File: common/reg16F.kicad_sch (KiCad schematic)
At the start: 8 parts, among them U17 74AHC1G08, U18 SN74AHC16374DGGR

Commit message: Updated ALU and moved common schematics to common/ for enhanced reusability
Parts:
- U17: footprint Package_TO_SOT_SMD:SOT-353_SC-70-5 -> Package_TO_SOT_SMD:SOT-23-5
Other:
- title: (none) -> 16-bit Register
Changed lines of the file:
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@@
 	(paper "A4")
 	(title_block
+		(title "16-bit Register")
 		(rev "V1.0")
+		(comment 1 "Designed to be used as a drop-in replacement to 4 74LS173 ICs used together")
 	)
 	(junction
@@
 		)
 		(instances
-			(project ""
+			(project "ALU"
 				(path "/c0bb03ae-ed0c-4e9e-9f7c-15f29fb8b868/e88f18b5-e72c-4b0e-9142-9a24ab457305"
 					(reference "TP2")
@@
 			)
 		)
-		(property "Footprint" "Package_TO_SOT_SMD:SOT-353_SC-70-5"
+		(property "Footprint" "Package_TO_SOT_SMD:SOT-23-5"
 			(at 81.915 126.365 0)
 			(effects

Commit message: Made tri-state and register schematic look nice
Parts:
- removed U18: SN74AHC16374DGGR, Package_SO:TSSOP-48_6.1x12.5mm_P0.5mm, symbol 74FCT16374CTPVG:74FCT16374CTPVG
- added U2: SN74AHCT16374DGGR, Package_SO:TSSOP-48_6.1x12.5mm_P0.5mm, symbol 74FCT16374CTPVG:74FCT16374CTPVG
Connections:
- net +5V: now also U2.18 (VCC_2), U2.31 (VCC), U2.42 (VCC_4), U2.7 (VCC_1)
- net DIN0: now also U2.23 (2Q8)
- net DIN1: now also U2.22 (2Q7)
- net DIN10: now also U2.9 (1Q6)
- net DIN11: now also U2.8 (1Q5)
- net DIN12: now also U2.6 (1Q4)
- net DIN13: now also U2.5 (1Q3)
- net DIN14: now also U2.3 (1Q2)
- net DIN15: now also U2.2 (1Q1)
- net DIN2: now also U2.20 (2Q6)
- net DIN3: now also U2.19 (2Q5)
- net DIN4: now also U2.17 (2Q4)
- net DIN5: now also U2.16 (2Q3)
- net DIN6: now also U2.14 (2Q2)
- net DIN7: now also U2.13 (2Q1)
- net DIN8: now also U2.12 (1Q8)
- net DIN9: now also U2.11 (1Q7)
- net DOUT0: now also U2.26 (2D8)
- net DOUT1: now also U2.27 (2D7)
- net DOUT10: now also U2.40 (1D6)
- net DOUT11: now also U2.41 (1D5)
- net DOUT12: now also U2.43 (1D4)
- net DOUT13: now also U2.44 (1D3)
- net DOUT14: now also U2.46 (1D2)
- net DOUT15: now also U2.47 (1D1)
- net DOUT2: now also U2.29 (2D6)
- net DOUT3: now also U2.30 (2D5)
- net DOUT4: now also U2.32 (2D4)
- net DOUT5: now also U2.33 (2D3)
- net DOUT6: now also U2.35 (2D2)
- net DOUT7: now also U2.36 (2D1)
- net DOUT8: now also U2.37 (1D8)
- net DOUT9: now also U2.38 (1D7)
- net GND: now also U2.10 (GND_2), U2.15 (GND_3), U2.21 (GND_4), U2.28 (GND), U2.34 (GND_6), U2.39 (GND_7), U2.4 (GND_1), U2.45 (GND_8)
- net ~{OE}: now also U2.25 (2CLK), U2.48 (1CLK)
- net at TP2.1, U17.4: now also U2.1 (1~{OE}), U2.24 (2~{OE})
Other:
- moved on the sheet: C24, C25, C26, C27, C28, TP2, U17

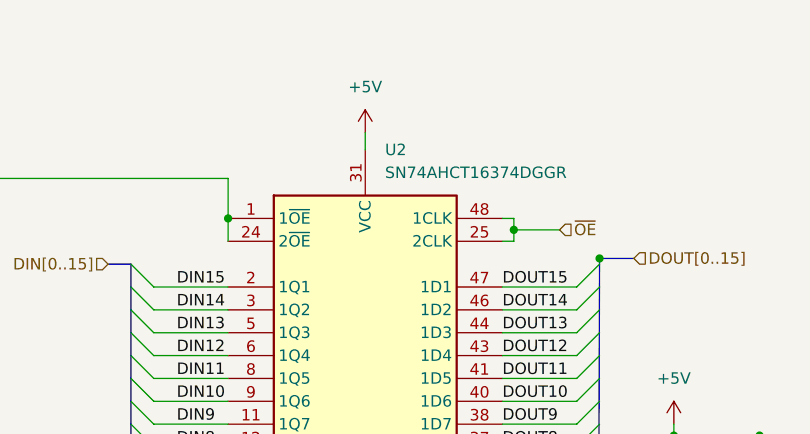
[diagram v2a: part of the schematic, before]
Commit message: Fixed silkscreen on ALU and Double Buffer
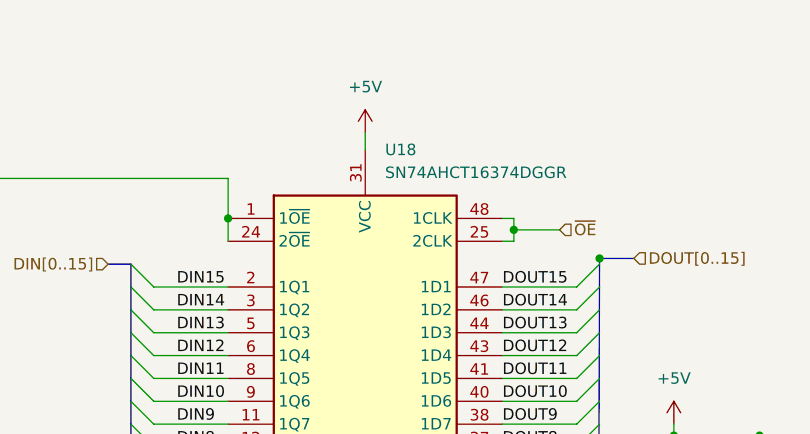
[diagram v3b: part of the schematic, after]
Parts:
- renumbered U2 to U18
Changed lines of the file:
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@@
 		(dnp no)
 		(fields_autoplaced yes)
-		(property "Reference" "#PWR040"
+		(property "Reference" "#PWR041"
 			(at 107.315 116.84 0)
 			(effects
@@
 		(dnp no)
 		(fields_autoplaced yes)
-		(property "Reference" "U2"
+		(property "Reference" "U18"
 			(at 109.5091 48.26 0)
 			(effects
@@
 		(dnp no)
 		(fields_autoplaced yes)
-		(property "Reference" "#PWR036"
+		(property "Reference" "#PWR037"
 			(at 107.315 50.165 0)
 			(effects

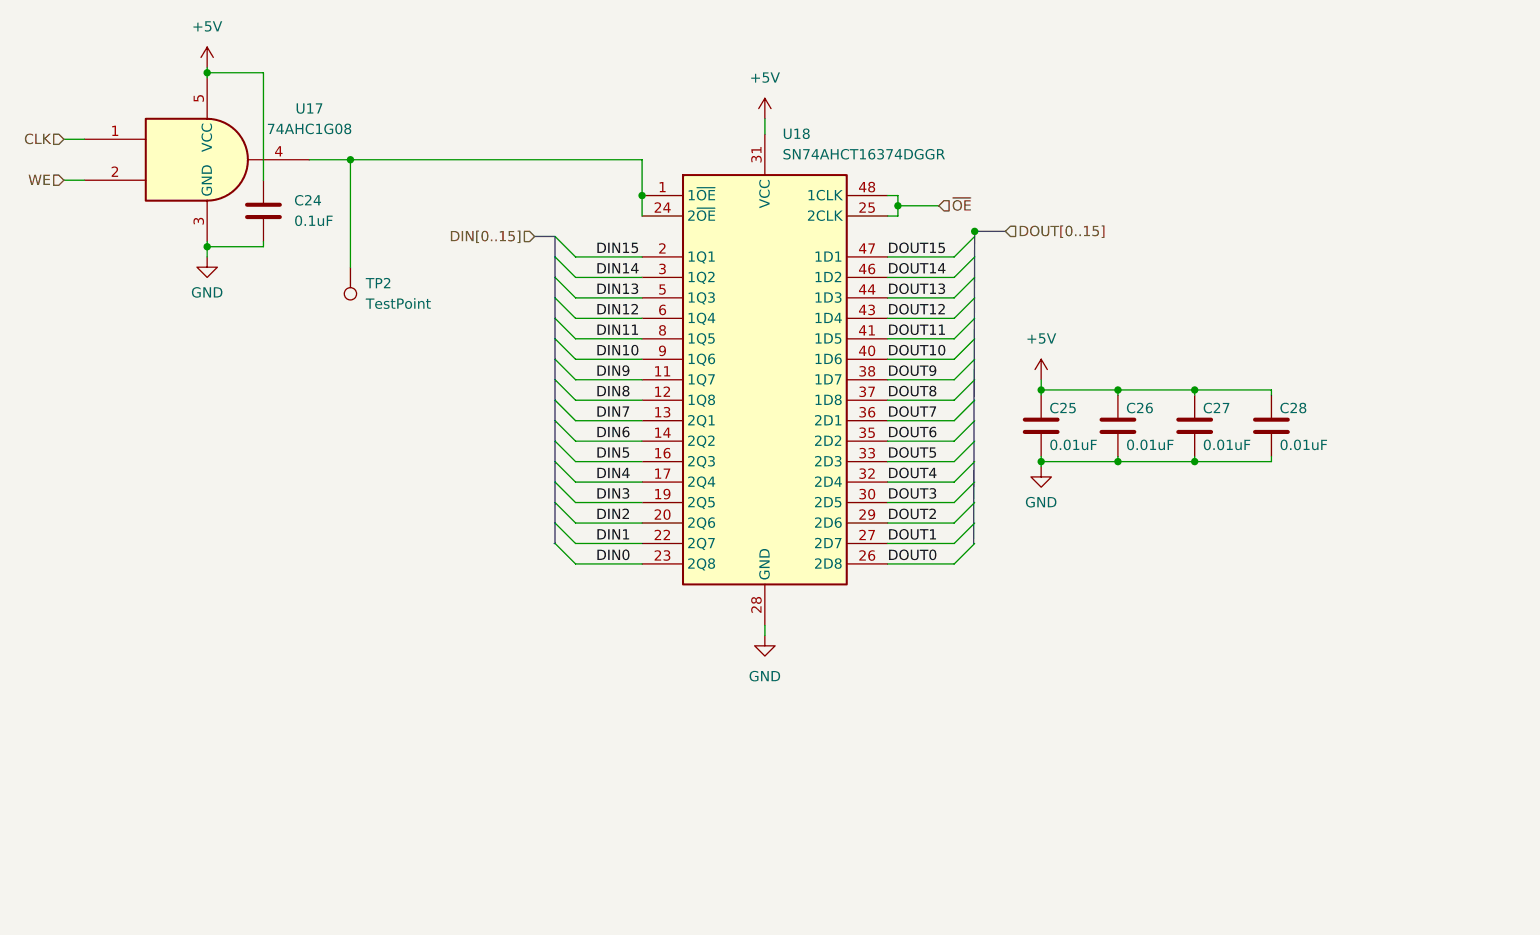
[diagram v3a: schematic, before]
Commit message: Fixed incorrect wiring in ALU (input registers)
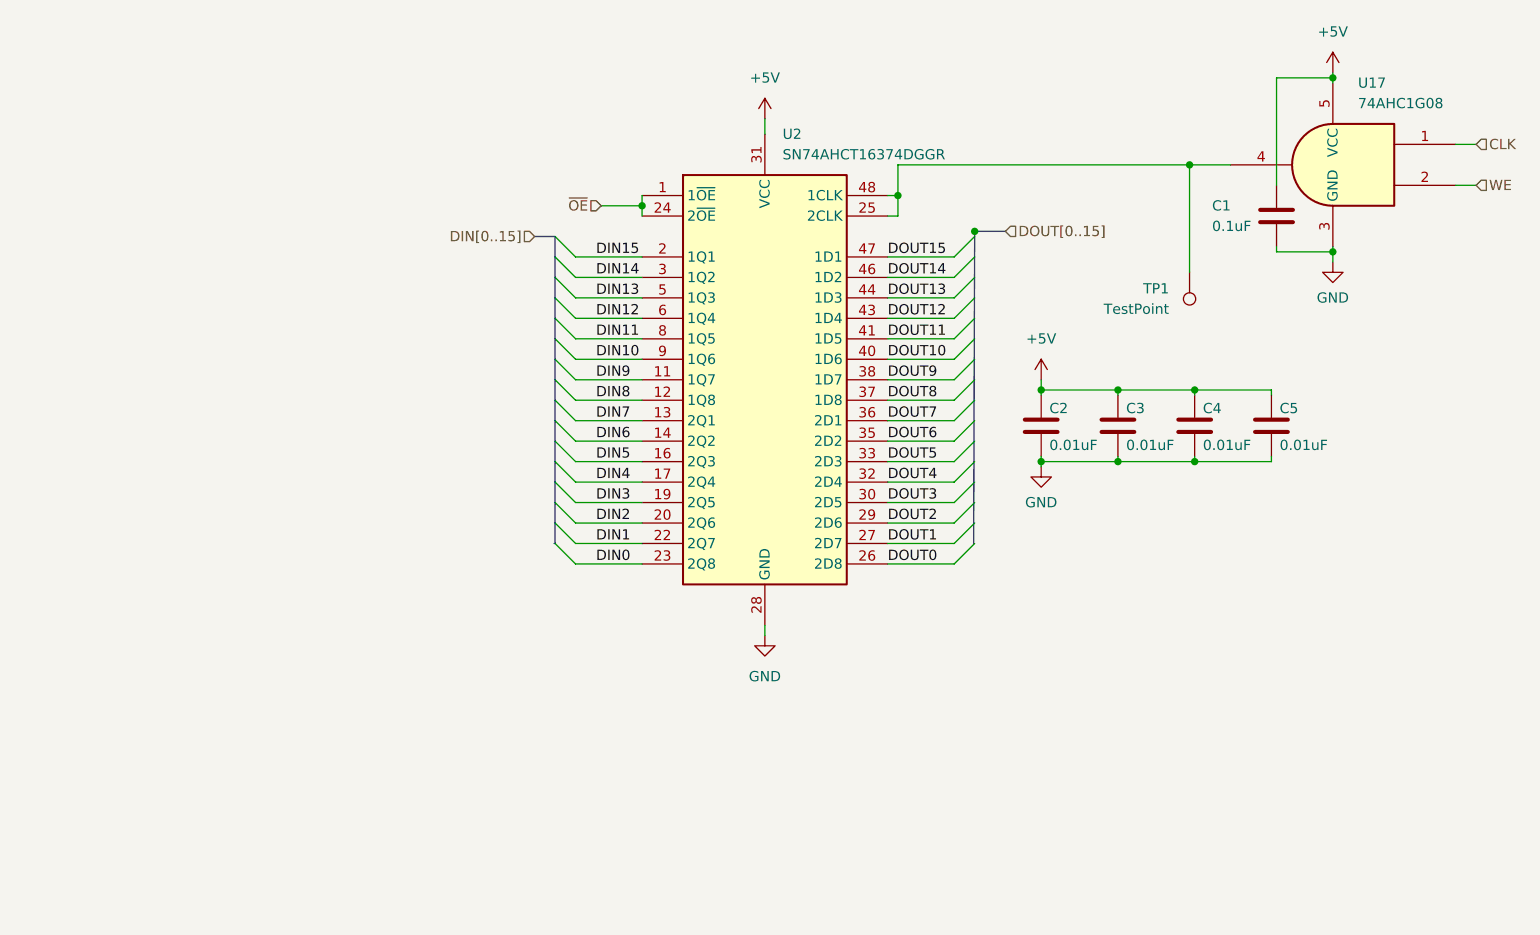
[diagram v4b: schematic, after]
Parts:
- renumbered C24 to C1, C25 to C2, C26 to C3, C27 to C4, C28 to C5, TP2 to TP1, U18 to U2
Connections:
- net ~{OE}: now also U2.1 (1~{OE}), U2.24 (2~{OE}); no longer U2.25 (2CLK), U2.48 (1CLK)
- net at TP1.1, U17.4: now also U2.25 (2CLK), U2.48 (1CLK); no longer U2.1 (1~{OE}), U2.24 (2~{OE})
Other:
- moved on the sheet: C1, TP1, U17

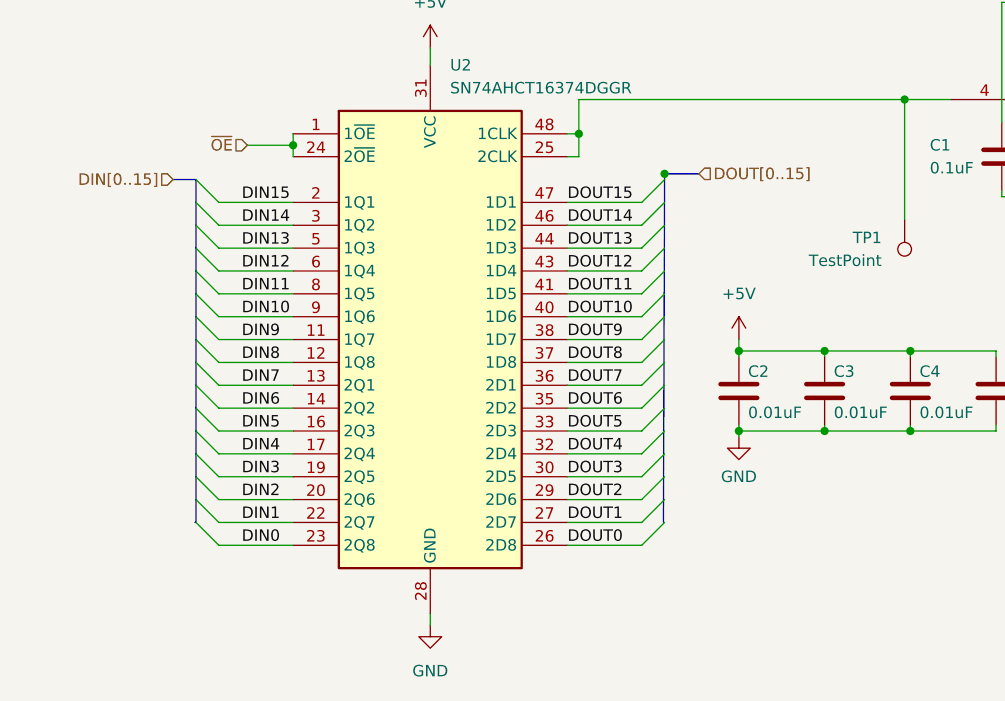
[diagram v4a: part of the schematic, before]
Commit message: Fixed register data flow direction and added mounitng holes to ALU
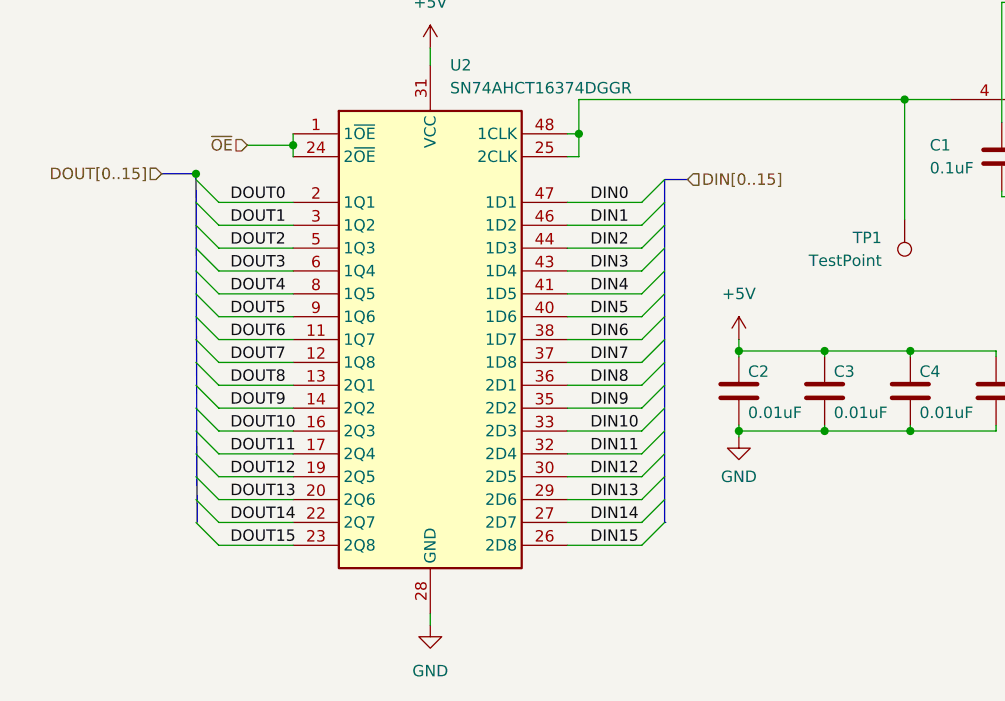
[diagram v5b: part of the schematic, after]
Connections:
- net DIN0: now also U2.47 (1D1); no longer U2.23 (2Q8)
- net DIN1: now also U2.46 (1D2); no longer U2.22 (2Q7)
- net DIN10: now also U2.33 (2D3); no longer U2.9 (1Q6)
- net DIN11: now also U2.32 (2D4); no longer U2.8 (1Q5)
- net DIN12: now also U2.30 (2D5); no longer U2.6 (1Q4)
- net DIN13: now also U2.29 (2D6); no longer U2.5 (1Q3)
- net DIN14: now also U2.27 (2D7); no longer U2.3 (1Q2)
- net DIN15: now also U2.26 (2D8); no longer U2.2 (1Q1)
- net DIN2: now also U2.44 (1D3); no longer U2.20 (2Q6)
- net DIN3: now also U2.43 (1D4); no longer U2.19 (2Q5)
- net DIN4: now also U2.41 (1D5); no longer U2.17 (2Q4)
- net DIN5: now also U2.40 (1D6); no longer U2.16 (2Q3)
- net DIN6: now also U2.38 (1D7); no longer U2.14 (2Q2)
- net DIN7: now also U2.37 (1D8); no longer U2.13 (2Q1)
- net DIN8: now also U2.36 (2D1); no longer U2.12 (1Q8)
- net DIN9: now also U2.35 (2D2); no longer U2.11 (1Q7)
- net DOUT0: now also U2.2 (1Q1); no longer U2.26 (2D8)
- net DOUT1: now also U2.3 (1Q2); no longer U2.27 (2D7)
- net DOUT10: now also U2.16 (2Q3); no longer U2.40 (1D6)
- net DOUT11: now also U2.17 (2Q4); no longer U2.41 (1D5)
- net DOUT12: now also U2.19 (2Q5); no longer U2.43 (1D4)
- net DOUT13: now also U2.20 (2Q6); no longer U2.44 (1D3)
- net DOUT14: now also U2.22 (2Q7); no longer U2.46 (1D2)
- net DOUT15: now also U2.23 (2Q8); no longer U2.47 (1D1)
- net DOUT2: now also U2.5 (1Q3); no longer U2.29 (2D6)
- net DOUT3: now also U2.6 (1Q4); no longer U2.30 (2D5)
- net DOUT4: now also U2.8 (1Q5); no longer U2.32 (2D4)
- net DOUT5: now also U2.9 (1Q6); no longer U2.33 (2D3)
- net DOUT6: now also U2.11 (1Q7); no longer U2.35 (2D2)
- net DOUT7: now also U2.12 (1Q8); no longer U2.36 (2D1)
- net DOUT8: now also U2.13 (2Q1); no longer U2.37 (1D8)
- net DOUT9: now also U2.14 (2Q2); no longer U2.38 (1D7)
